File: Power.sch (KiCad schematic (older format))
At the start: 22 parts, among them CON2 BARREL_JACK, IC1 LD1117S33, IC2 LM25011

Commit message: #3 Add SD card interface #4 Add CAN & UART transceivers
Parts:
- removed C13, C35: 10u, ~, symbol CP1
- removed C14, C16: 100n, ~, symbol C
- removed C15: 22n, ~, symbol C
- removed C17: 22u, ~, symbol CP1
- removed C34: 1u, ~, symbol C
- removed CON2: BARREL_JACK, symbol BARREL_JACK
- removed D1, D2, D3, D4, D5: DIODESCH, ~, symbol DIODESCH
- removed IC1: LD1117S33, ~, symbol LD1117S33
- removed IC2: LM25011, symbol LM25011
- removed JP2: JUMPER, ~, symbol JUMPER
- removed R10, R7, R9: 10k, ~, symbol R
- removed R6: 158k, ~, symbol R
- removed R8: 0R075, ~, symbol R
- added C11: 4u7, ~, symbol C-RESCUE-Noodleboard
- added C12: 10u, ~, symbol C-RESCUE-Noodleboard
- added C13: 1u, ~, symbol C-RESCUE-Noodleboard
- added C14: 100n, ~, symbol C-RESCUE-Noodleboard
- added L1: 2u2, symbol INDUCTOR
- added U1: TPS62291DRVT, symbol TPS62291DRVT
- L2: value MSS1038-153MLC -> fcm1608
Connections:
- net labels added: VDDA
- net labels removed: 5V, MCU_3V3, MCU_3V30, VBUS_FS_0, VBUS_HS_0, VIN
- wire segments 62 -> 21
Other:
- note added: "Power"

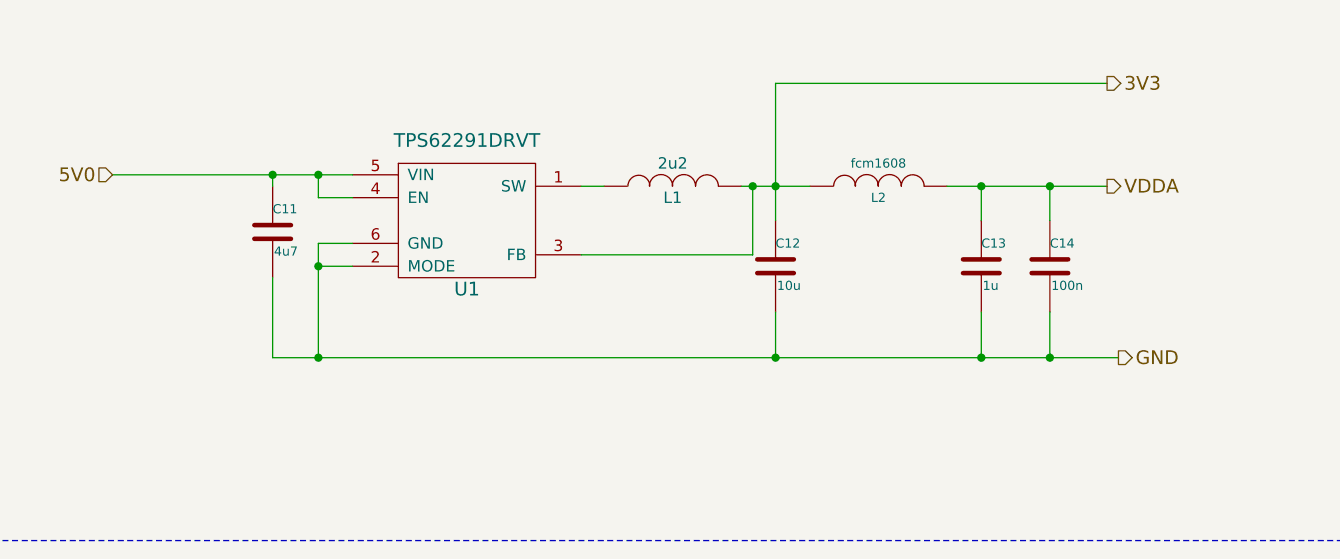
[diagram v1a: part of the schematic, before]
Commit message: - New PCB design  - Updated last schematics modifications  - Added Gerber outputs (old and new version)
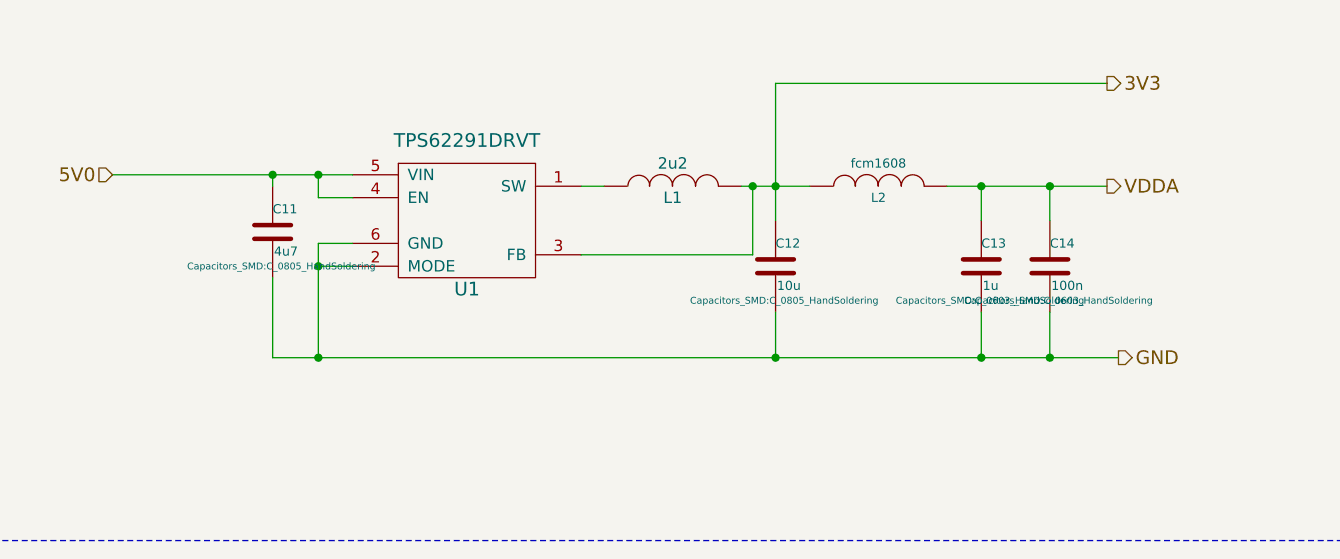
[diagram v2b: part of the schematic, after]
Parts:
- C11, C12: footprint ~ -> Capacitors_SMD:C_0805_HandSoldering
- C13, C14: footprint ~ -> Capacitors_SMD:C_0603_HandSoldering
- L1: footprint (none) -> ComponentLibv2:SMD_1008
- L2: footprint ~ -> Resistors_SMD:R_0603_HandSoldering
- U1: footprint (none) -> ComponentLibv2:S-PWSON-N6
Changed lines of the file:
@@
 F 0 "L2" V 6550 4000 40  0000 C CNN
 F 1 "fcm1608" V 6700 4000 40  0000 C CNN
-F 2 "~" H 6600 4000 60  0000 C CNN
+F 2 "Resistors_SMD:R_0603_HandSoldering" H 6600 4000 60  0001 C CNN
 F 3 "~" H 6600 4000 60  0000 C CNN
 	1    6600 4000
@@
 F 0 "C14" H 7350 4450 40  0000 L CNN
 F 1 "100n" H 7356 4265 40  0000 L CNN
-F 2 "~" H 7388 4200 30  0000 C CNN
+F 2 "Capacitors_SMD:C_0603_HandSoldering" H 7388 4200 30  0000 C CNN
 F 3 "~" H 7350 4350 60  0000 C CNN
 	1    7350 4350
@@
 F 0 "C11" H 3950 4300 40  0000 L CNN
 F 1 "4u7" H 3956 4115 40  0000 L CNN
-F 2 "~" H 3988 4050 30  0000 C CNN
+F 2 "Capacitors_SMD:C_0805_HandSoldering" H 3988 4050 30  0000 C CNN
 F 3 "http://www.farnell.com/datasheets/1784405.pdf" H 3950 4200 60  0001 C CNN
 F 4 "GRM188R60J475KE19D" H 3950 4200 60  0001 C CNN "Part Number"
@@
 F 0 "C12" H 6150 4450 40  0000 L CNN
 F 1 "10u" H 6156 4265 40  0000 L CNN
-F 2 "~" H 6188 4200 30  0000 C CNN
+F 2 "Capacitors_SMD:C_0805_HandSoldering" H 6188 4200 30  0000 C CNN
 F 3 "http://www.farnell.com/datasheets/1796654.pdf" H 6150 4350 60  0001 C CNN
 F 4 "C1608X5R0J106M" H 6150 4350 60  0001 C CNN "Part Number"
@@
 F 0 "C13" H 7050 4450 40  0000 L CNN
 F 1 "1u" H 7056 4265 40  0000 L CNN
-F 2 "~" H 7088 4200 30  0000 C CNN
+F 2 "Capacitors_SMD:C_0603_HandSoldering" H 7088 4200 30  0000 C CNN
 F 3 "~" H 7050 4350 60  0000 C CNN
 	1    7050 4350
@@
 F 0 "L1" V 5650 4000 50  0000 C CNN
 F 1 "2u2" V 5800 4000 50  0000 C CNN
-F 2 "" H 5700 4000 60  0000 C CNN
+F 2 "ComponentLibv2:SMD_1008" H 5700 4000 60  0001 C CNN
 F 3 "http://katalog.we-online.de/pbs/datasheet/74479887222.pdf" H 5700 4000 60  0001 C CNN
 F 4 "74479887222A" V 5700 4000 60  0001 C CNN "Part Number"
@@
 F 0 "U1" H 4800 3850 60  0000 C CNN
 F 1 "TPS62291DRVT" H 4800 4500 60  0000 C CNN
-F 2 "" H 4800 4150 60  0000 C CNN
+F 2 "ComponentLibv2:S-PWSON-N6" H 4800 4150 60  0001 C CNN
 F 3 "" H 4800 4150 60  0000 C CNN
 	1    4800 4150

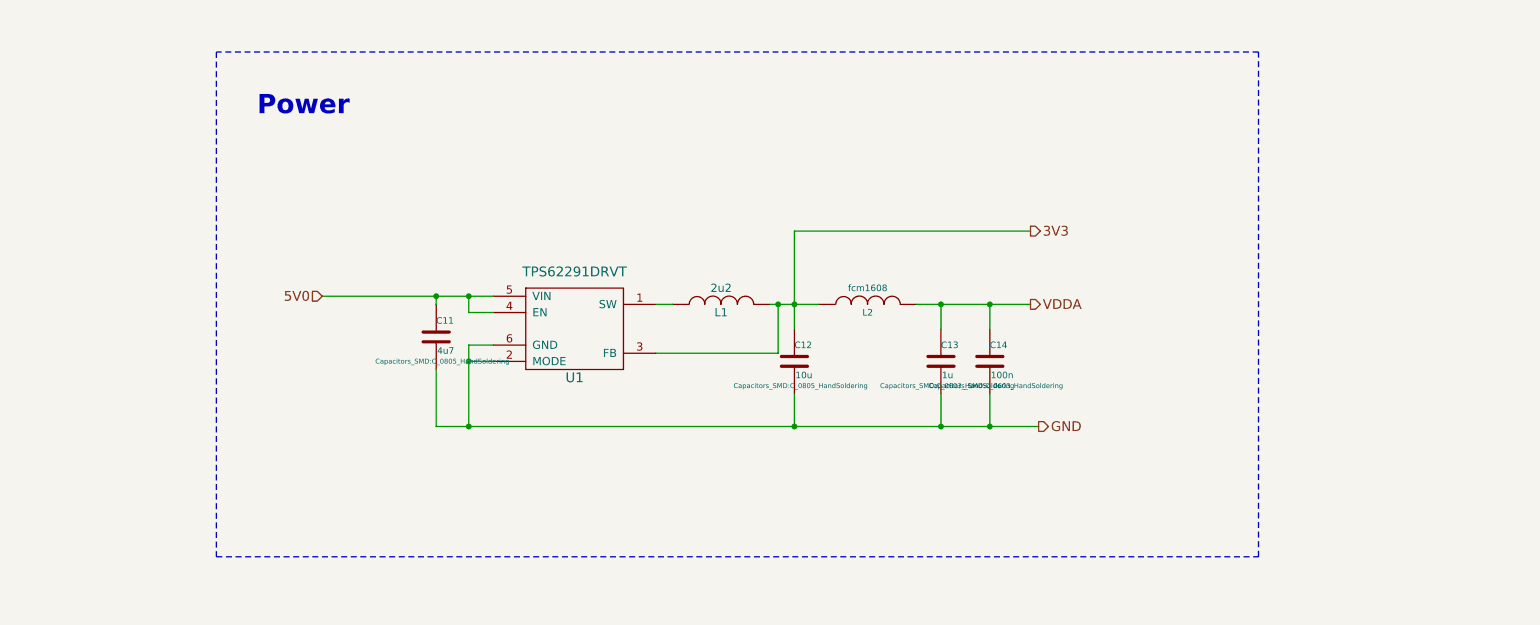
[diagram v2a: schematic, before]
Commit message: #5 Review USB power supply #6 Power signaling LED should be in power sheet - Simplified outputs (Gerber, sch & pcb)
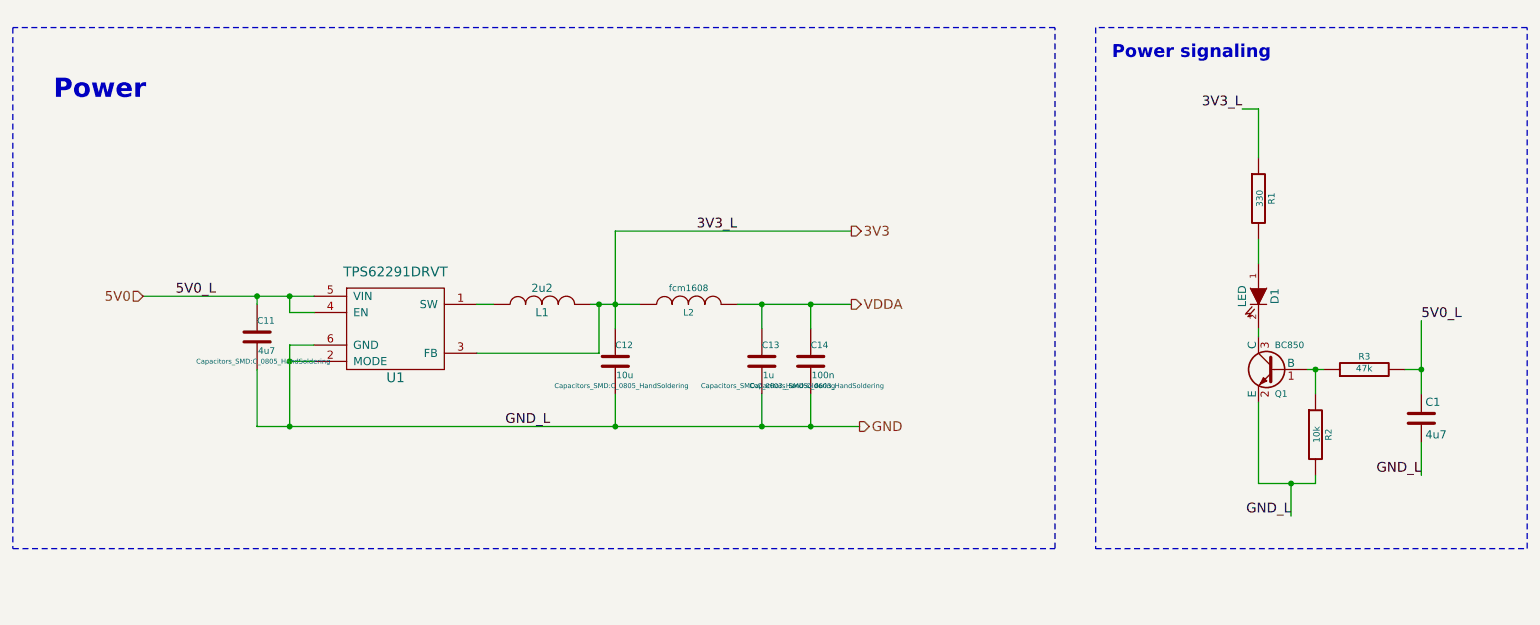
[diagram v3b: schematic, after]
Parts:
- added C1: 4u7, Capacitors_SMD:C_0805_HandSoldering, symbol C
- added D1: LED, LEDs:LED-0805, symbol LED-RESCUE-Noodleboard
- added Q1: BC850, TO_SOT_Packages_SMD:SOT-23_Handsoldering, symbol BC850
- added R1: 330, Resistors_SMD:R_0603_HandSoldering, symbol R-RESCUE-Noodleboard
- added R2: 10k, Resistors_SMD:R_0603_HandSoldering, symbol R-RESCUE-Noodleboard
- added R3: 47k, Resistors_SMD:R_0603_HandSoldering, symbol R-RESCUE-Noodleboard
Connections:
- net 3V3: now also R1.1
- net 5V0: now also C1.1, R3.2
- net GND: now also C1.2, Q1.2 (E), R2.2
- new net: D1.1 (A), R1.2
- new net: D1.2 (K), Q1.3 (C)
- new net: Q1.1 (B), R2.1, R3.1
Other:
- note added: "Power signaling\n"
- moved on the sheet: C11, C12, C13, C14, L1, L2, U1
